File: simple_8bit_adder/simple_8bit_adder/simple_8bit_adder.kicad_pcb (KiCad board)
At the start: 2 copper layers, 40.1 x 37.5 mm, 51 parts, among them Q10 2N7002, Q10_0 2N7002, Q10_1 2N7002, Q11 2N7002, Q11_0 2N7002, Q15_0 2N7002, Q15_1 2N7002, Q15_2 2N7002, Q15_3 2N7002, Q19_0 2N7002, Q19_1 2N7002, Q1_0 2N7002, Q20_0 2N7002, Q20_1 2N7002, Q22_0 2N7002, Q22_1 2N7002, Q22_2 2N7002, Q29_0 2N7002, Q29_1 2N7002, Q29_2 2N7002, Q2_0 2N7002, Q3_0 2N7002, Q3_1 2N7002, Q46_0 2N7002, Q46_1 2N7002, Q47_0 2N7002, Q47_1 2N7002, Q4_0 2N7002, Q5_0 2N7002, Q6_0 2N7002, Q6_1 2N7002, Q7_0 2N7002, Q8 2N7002

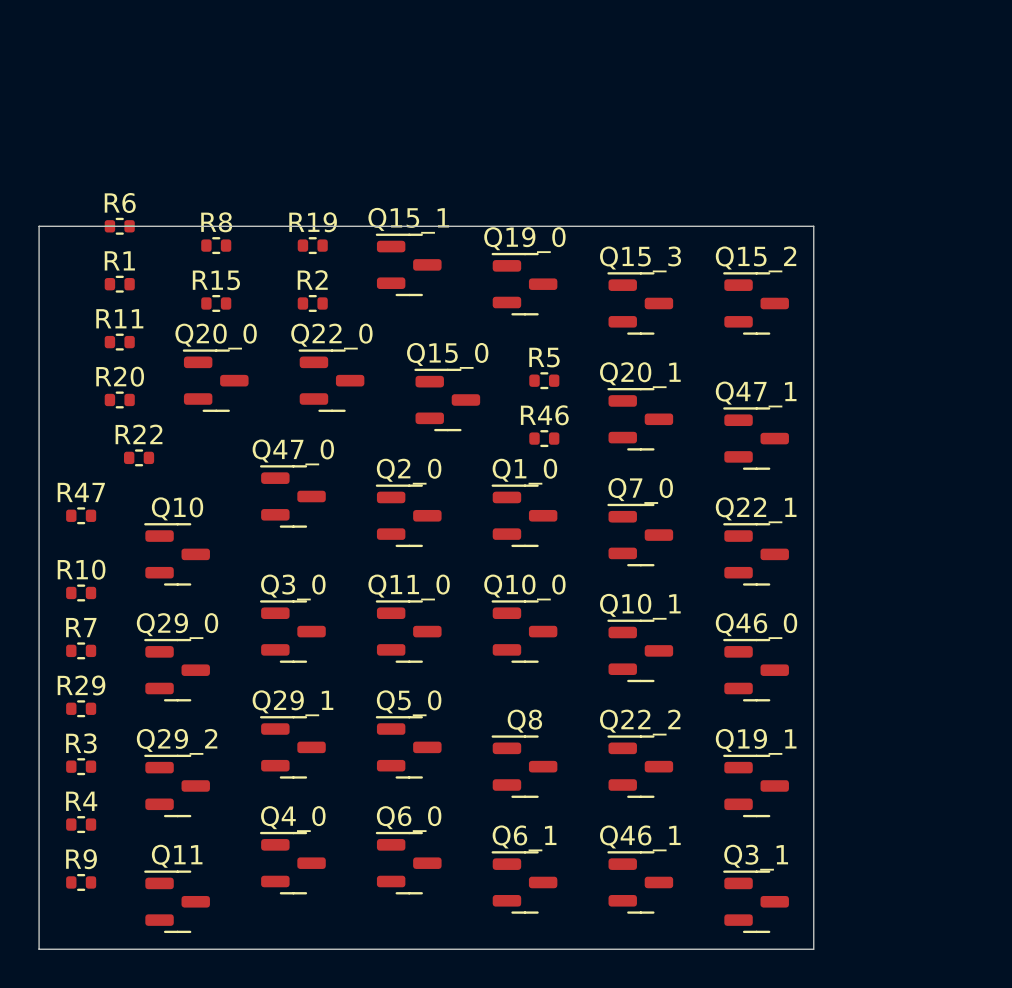
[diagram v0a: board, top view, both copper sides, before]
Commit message: added example files
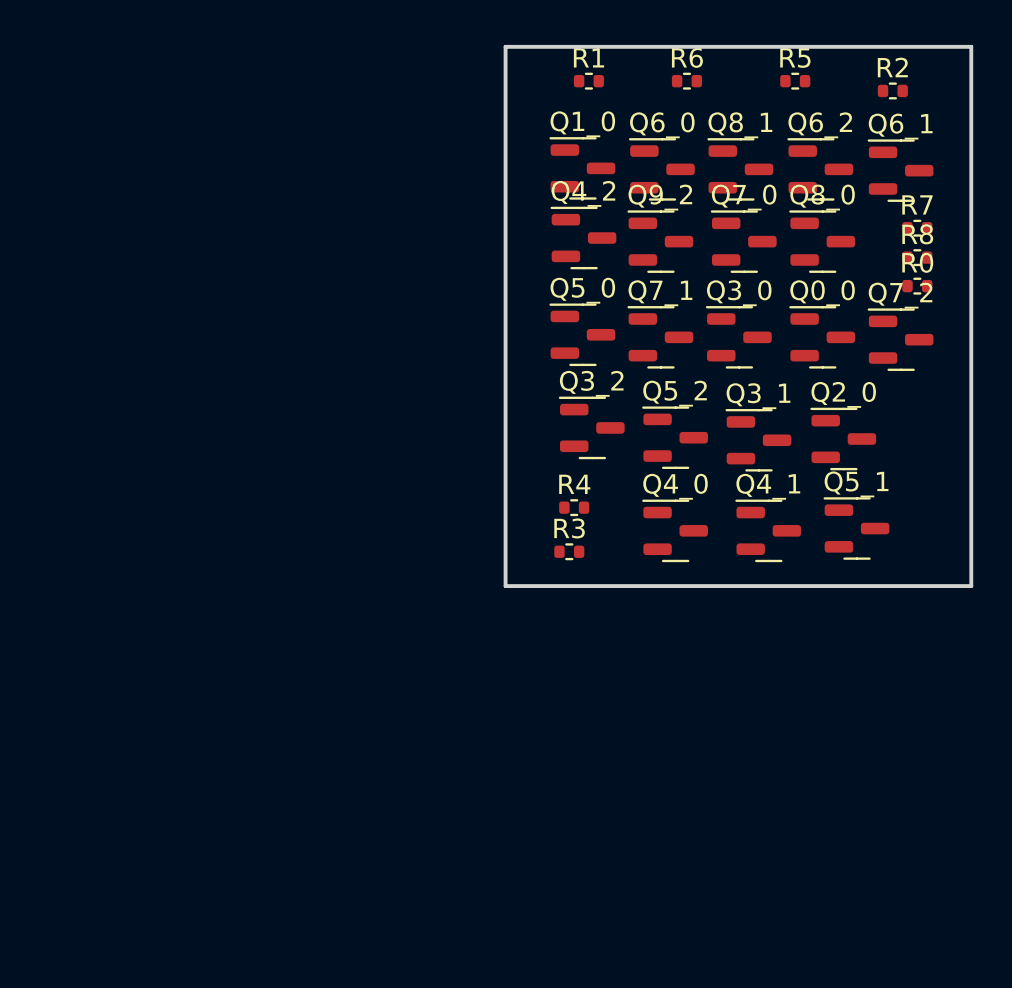
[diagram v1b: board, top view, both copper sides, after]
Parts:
- removed Q10, Q10_0, Q10_1, Q11, Q11_0, Q15_0, Q15_1, Q15_2, Q15_3, Q19_0, Q19_1, Q20_0, Q20_1, Q22_0, Q22_1, Q22_2, Q29_0, Q29_1, Q29_2, Q46_0, Q46_1, Q47_0, Q47_1, Q8: 2N7002, Package_TO_SOT_SMD:SOT-23
- removed R10, R11, R15, R19, R20, R22, R29, R46, R47, R9: R_Small, Resistor_SMD:R_0402_1005Metric
- added Q0_0: 2N7002, Package_TO_SOT_SMD:SOT-23, F.Cu at (79.4, 43.8)
- added Q3_2: 2N7002, Package_TO_SOT_SMD:SOT-23, F.Cu at (67.5, 48.4)
- added Q4_1: 2N7002, Package_TO_SOT_SMD:SOT-23, F.Cu at (76.6, 53.8)
- added Q4_2: 2N7002, Package_TO_SOT_SMD:SOT-23, F.Cu at (67.1, 38.6)
- added Q5_1: 2N7002, Package_TO_SOT_SMD:SOT-23, F.Cu at (81.2, 53.7)
- added Q5_2: 2N7002, Package_TO_SOT_SMD:SOT-23, F.Cu at (71.8, 49.0)
- added Q6_2: 2N7002, Package_TO_SOT_SMD:SOT-23, F.Cu at (79.3, 35.1)
- added Q7_1: 2N7002, Package_TO_SOT_SMD:SOT-23, F.Cu at (71.0, 43.8)
- added Q7_2: 2N7002, Package_TO_SOT_SMD:SOT-23, F.Cu at (83.5, 43.9)
- added Q8_0: 2N7002, Package_TO_SOT_SMD:SOT-23, F.Cu at (79.4, 38.8)
- added Q8_1: 2N7002, Package_TO_SOT_SMD:SOT-23, F.Cu at (75.2, 35.1)
- added Q9_2: 2N7002, Package_TO_SOT_SMD:SOT-23, F.Cu at (71.0, 38.8)
- added R0: R_Small, Resistor_SMD:R_0402_1005Metric, F.Cu at (84.3, 41.1)
- moved R7 48.5 mm to (84.3, 38.1)
- moved Q6_1 41.7 mm to (83.5, 35.1)
- moved Q6_0 38.3 mm to (71.1, 35.1)
- moved R8 36.3 mm to (84.3, 39.6)
- moved R2 32.0 mm to (83.1, 31.0)
- moved R4 30.4 mm to (66.5, 52.6)
- moved R6 30.3 mm to (72.4, 30.5)
- moved Q3_0 27.7 mm to (75.1, 43.8)
- moved R3 27.6 mm to (66.3, 54.9)
- moved R1 26.5 mm to (67.3, 30.5)
- moved Q4_0 26.2 mm to (71.8, 53.8)
- moved Q3_1 23.9 mm to (76.1, 49.1)
- moved Q5_0 23.2 mm to (67.0, 43.6)
- moved Q2_0 22.9 mm to (80.5, 49.0)
- moved R5 20.2 mm to (78.0, 30.5)
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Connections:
- net /Bnot renamed /Q2
- net /Cnot renamed /Q1
- Q1_0 pad 1: /C -> /DATA
- Q2_0 pad 1: /B -> /RST
- Q3_0 pad 1: /Anot -> /Q0
- Q3_1 pad 1: /Dnot -> /NAND6
- Q3_1 pad 2: GND -> Net-(Q3_1-S)
- Q4_0 pad 2: GND -> Net-(Q4_0-S)
- Q4_0 pad 3: /NAND3_not -> /NAND4
- Q5_0 pad 1: /D -> /NAND4
- Q5_0 pad 2: GND -> Net-(Q5_0-S)
- Q5_0 pad 3: /Dnot -> /NAND5
- Q6_0 pad 1: /NAND3_not -> /NAND5
- Q6_1 pad 1: /Dnot -> /DATA
- Q6_1 pad 2: GND -> Net-(Q6_1-S)
- Q7_0 pad 1: /A -> /Q0
- Q7_0 pad 2: GND -> Net-(Q7_0-S)
- Q7_0 pad 3: /Anot -> /Q
- R4 pad 2: /NAND3_not -> /NAND4
- R5 pad 2: /Dnot -> /NAND5
- R7 pad 2: /Anot -> /Q
- R8 pad 2: /Q -> /Q_NOT
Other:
- board size 40.1 x 37.5 mm -> 24.1 x 27.9 mm
